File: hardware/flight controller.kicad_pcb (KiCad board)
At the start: 4 copper layers, 50.2 x 98.1 mm, 98 parts, among them J1 Input Power, J10 M8, J11 M9, J12 M10, J13 M11, J14 M12, J15 I2C4, J16 Video In, J17 Video Out, J18 LED Strip, J19 USB_C_Receptacle_USB2.0_16P, J2 M1, J20 UART2, J21 UART7, J22 UART5, J23 UART8, J24 GPIO, J25 SWD, J26 UART3, J27 UART4, J3 M2, J4 M3, J5 M4, J6 M5, J7 M6, J8 Micro_SD_Card, J9 M7, U1 TPS54302, U2 BMP388, U3 QMC5883P, U4 STM32H743VITx, U5 AT7456E, U6 ICM-42688-P, Y1 27MHz, Y2 16MHz, Y3 32.768kHz

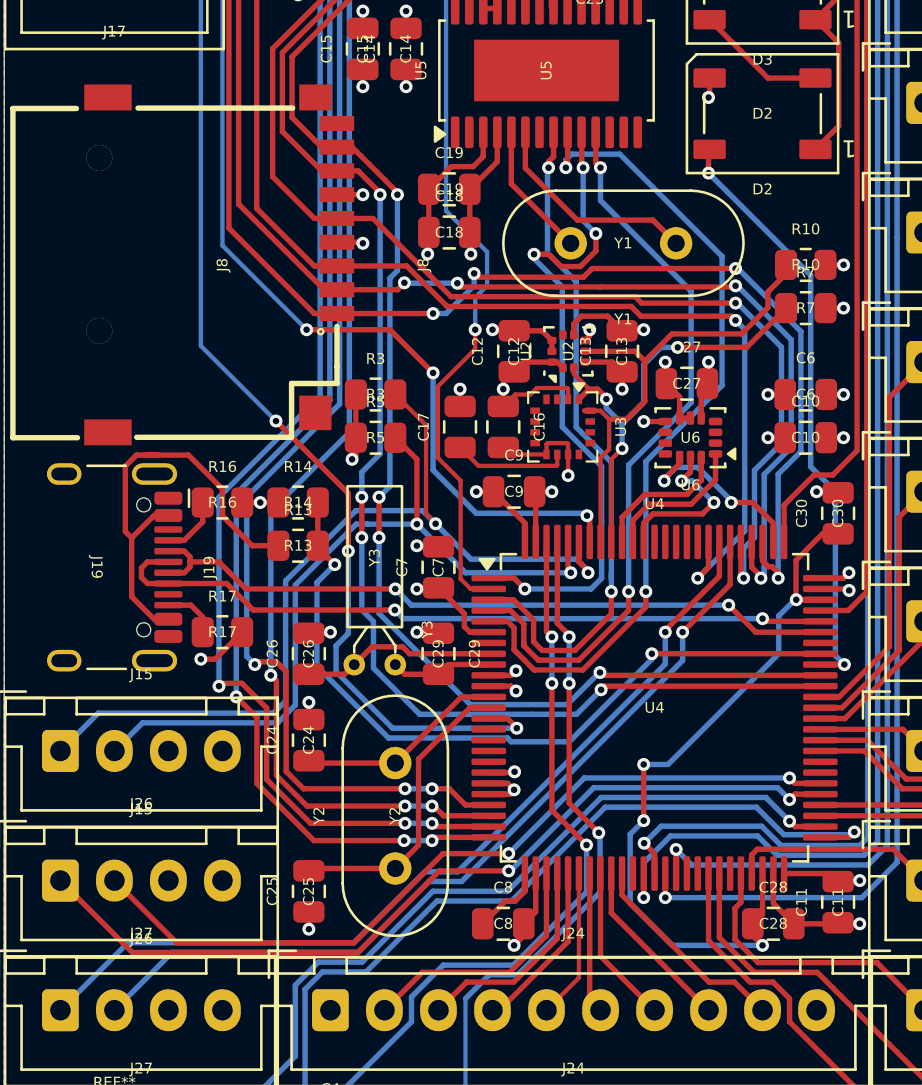
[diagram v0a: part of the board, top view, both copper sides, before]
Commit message: smd crystal
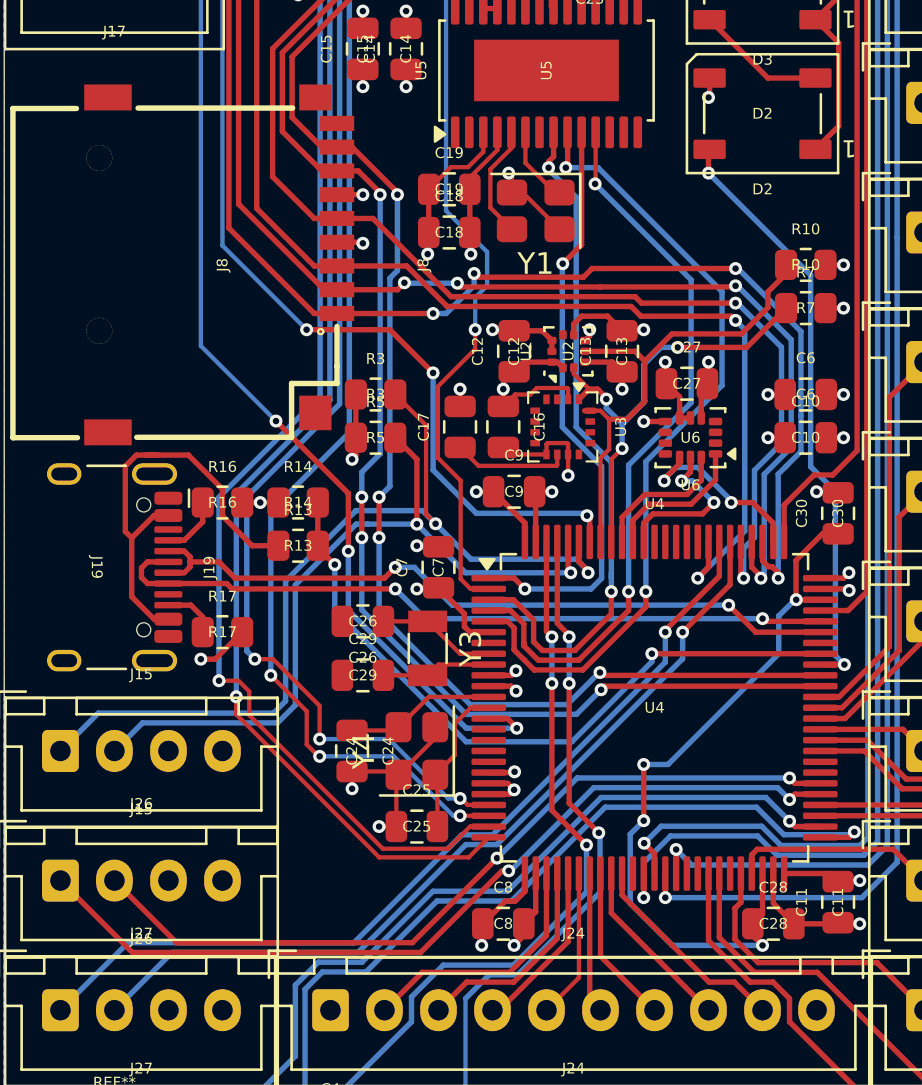
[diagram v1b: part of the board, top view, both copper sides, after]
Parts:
- removed Y2: 16MHz, Crystal:Crystal_HC49-U_Vertical
- added Y4: 16MHz, Crystal:Crystal_SMD_3225-4Pin_3.2x2.5mm, F.Cu at (141.0, 126.5)
- C24, C25: value 33pF -> 12pF
- C26, C29: value 15pF -> 18pF
- Y1: value 27MHz -> Crystal_GND24; footprint Crystal:Crystal_HC49-U_Vertical -> Crystal:Crystal_SMD_3225-4Pin_3.2x2.5mm
- Y3: footprint Crystal:Crystal_DS26_D2.0mm_L6.0mm_Horizontal -> Crystal:Crystal_SMD_3215-2Pin_3.2x1.5mm
- moved Y1 6.67 mm to (146.5, 101.5)
- moved C25 5.83 mm to (141.0, 130.0), turned to 0 degrees
- moved C29 3.64 mm to (138.5, 123.0), turned to 0 degrees
- moved C26 2.92 mm to (138.5, 120.5), turned to 180 degrees
- moved C24 2.06 mm to (138.0, 126.5), turned to -90 degrees
- moved Y3 1.68 mm to (141.5, 121.8), turned to -90 degrees
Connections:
- Y1 pad 2: Net-(U5-CLKIN) -> GND
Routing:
- net GND: track 71.3 -> 81.8 mm
- net /OSC_OUT: track 13.8 -> 7.06 mm
- net Net-(U5-XFB): track 10.1 -> 3.56 mm
- net /OSI_SCK: track 31.1 -> 27.4 mm, vias 4 -> 2
- net /OSC_32_IN: track 8.98 -> 5.50 mm
- net /OSC_IN: track 9.64 -> 6.97 mm
- net /VBUS_SENSE: track 34.8 -> 32.2 mm
- net /NRST: track 77.0 -> 74.6 mm
- net /UART2_CTS: track 91.6 -> 89.6 mm
- net /OSI_MOSI: track 39.0 -> 37.3 mm
- net /UART2_RTS: track 92.7 -> 91.0 mm
- net /SD_D0: track 61.5 -> 60.2 mm
- net Net-(U5-CLKIN): track 6.27 -> 5.31 mm
- net /UART2_TX: track 89.7 -> 89.0 mm, vias 3 -> 1
- net /UART2_RX: track 91.0 -> 90.3 mm, vias 3 -> 1

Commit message: smol
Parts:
- removed C12, C19, C21, C23: 100nF, Capacitor_SMD:C_0805_2012Metric
- removed C18: 1uF, Capacitor_SMD:C_0805_2012Metric
- removed C20: 470uF, Capacitor_THT:CP_Radial_D8.0mm_P3.50mm
- removed C22: 1000uF, Capacitor_THT:CP_Radial_D8.0mm_P3.50mm
- removed R15, R18: 75, Resistor_SMD:R_0805_2012Metric
- removed the REF** at (167.0, 78.5)
- removed the REF** at (167.0, 145.5)
- removed the REF** at (127.0, 145.5)
- removed the REF** at (127.0, 78.5)
- removed U5: AT7456E, Package_SO:TSSOP-28-1EP_4.4x9.7mm_P0.65mm_EP2.85x6.7mm
- removed Y1: Crystal_GND24, Crystal:Crystal_SMD_3225-4Pin_3.2x2.5mm
- added C31: 22uF, Capacitor_SMD:C_1206_3216Metric, B.Cu at (157.5, 60.0)
- added C32: 22uF, Capacitor_SMD:C_1206_3216Metric, B.Cu at (155.0, 60.0)
- added C33: 100nF, Capacitor_SMD:C_0603_1608Metric, B.Cu at (152.0, 63.0)
- added C34: 100nF, Capacitor_SMD:C_0603_1608Metric, B.Cu at (157.0, 69.0)
- added C35: 1uF, Capacitor_SMD:C_0603_1608Metric, B.Cu at (157.0, 70.5)
- added R22: 1K, Resistor_SMD:R_0603_1608Metric, B.Cu at (148.5, 66.0)
- added R23: 75, Resistor_SMD:R_0603_1608Metric, B.Cu at (152.0, 61.5)
- added R24: 75, Resistor_SMD:R_0603_1608Metric, B.Cu at (149.0, 63.0)
- added REF**: MountingHole_2.7mm_M2.5, MountingHole:MountingHole_2.7mm_M2.5, F.Cu at (142.5, 128.0)
- added U7: AT7456ELAH_C42388749, lcsc:LGA-16_L6.8-W4.0-P0.65-TL-2EP, B.Cu at (153.0, 66.1)
- added Y2: Crystal_GND24, Crystal:Crystal_SMD_3225-4Pin_3.2x2.5mm, B.Cu at (153.0, 70.0)
- C1, C13, C14, C15, C16, C27, C3, C6, C7, C8, C9: footprint Capacitor_SMD:C_0805_2012Metric -> Capacitor_SMD:C_0603_1608Metric
- C10, C11, C24, C25, C26, C28, C29, C30: footprint Capacitor_SMD:C_0805_2012Metric -> Capacitor_SMD:C_0603_1608Metric; moved to B.Cu
- D1: value 1N4001 -> SS54; footprint Diode_THT:D_DO-41_SOD81_P7.62mm_Horizontal -> Diode_SMD:D_SMA
- R1, R10, R11, R12, R13, R14, R16, R17, R20, R21, R3, R4, R5, R6, R7, R9: footprint Resistor_SMD:R_0805_2012Metric -> Resistor_SMD:R_0603_1608Metric; moved to B.Cu
- R19, R2, R8: footprint Resistor_SMD:R_0805_2012Metric -> Resistor_SMD:R_0603_1608Metric
- U4, Y3, Y4: moved to B.Cu
- moved C2 87.8 mm to (157.5, 71.5), turned to 180 degrees
- moved U1 84.4 mm to (157.5, 74.5), turned to 180 degrees
- moved C1 82.8 mm to (157.5, 77.0), turned to 180 degrees
- moved L1 78.4 mm to (151.0, 73.0), turned to 180 degrees
- moved C3 77.5 mm to (153.0, 77.5), turned to 0 degrees
- moved J22 75.5 mm to (167.5, 89.5)
- moved D5 75.4 mm to (85.9, 104.1), turned to 0 degrees
- moved J23 75.0 mm to (167.5, 96.0)
- moved R2 75.0 mm to (153.0, 80.5), turned to 0 degrees
- moved R8 73.0 mm to (153.0, 79.0), turned to 180 degrees
- moved D4 72.2 mm to (85.9, 97.5), turned to 0 degrees
- moved D3 71.1 mm to (85.9, 90.9), turned to 0 degrees
- moved J26 69.8 mm to (167.5, 77.5)
- moved J27 69.8 mm to (167.5, 83.5)
- moved C5 69.5 mm to (149.0, 78.0), turned to 0 degrees
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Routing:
- net +3.3V: track 91.6 -> 0.00 mm, vias 28 -> 0
- net /UART2_RTS: track 91.0 -> 0.00 mm, vias 3 -> 0
- net /UART2_RX: track 90.3 -> 0.00 mm, vias 1 -> 0
- net /UART2_CTS: track 89.6 -> 0.00 mm, vias 3 -> 0
- net /UART2_TX: track 89.0 -> 0.00 mm, vias 1 -> 0
- net /SWDIO: track 86.8 -> 0.00 mm
- net /SWCLK: track 82.8 -> 0.00 mm, vias 1 -> 0
- net GND: track 81.8 -> 0.00 mm, vias 37 -> 0
- net /UART7_RX: track 75.1 -> 0.00 mm, vias 1 -> 0
- net /NRST: track 74.6 -> 0.00 mm, vias 4 -> 0
- net /UART7_TX: track 73.8 -> 0.00 mm, vias 1 -> 0
- net /UART7_RTS: track 73.4 -> 0.00 mm, vias 1 -> 0
- net /UART7_CTS: track 71.8 -> 0.00 mm, vias 1 -> 0
- net /BOOT0: track 67.7 -> 0.00 mm, vias 4 -> 0
- net /SD_D2: track 60.9 -> 0.00 mm, vias 4 -> 0
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- removed copper zone on In2.Cu, net +3.3V
- removed copper zone on In2.Cu, net +5V
- removed copper zone on B.Cu, net GND
- removed copper zone on F.Cu, net GND
- removed copper zone on In1.Cu, net GND
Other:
- board size 50.2 x 98.1 mm -> 40 x 86.5 mm
- board text removed: "flight controller"

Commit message: idk
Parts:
- C6: moved to B.Cu
- moved R9 8.49 mm to (133.5, 89.5)
- moved R11 7.65 mm to (132.0, 91.0)
- moved R1 5.83 mm to (134.5, 87.5)
- moved C28 1.00 mm to (140.5, 87.5)
- moved C6 0.50 mm to (158.0, 81.0)
- moved C9 0.25 mm to (158.0, 97.8)
- moved U4 0.18 mm to (151.5, 90.5)
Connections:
- U4 pad 28: /A1 -> /A8
- U4 pad 29: /A2 -> /A7
- U4 pad 30: /A3 -> /A6
- U4 pad 31: /A4 -> /A1
- U4 pad 33: /A6 -> /A2
- U4 pad 34: /A7 -> /A4
- U4 pad 35: /A8 -> /A3
- U4 pad 43: /M1 -> /M4
- U4 pad 44: /M2 -> /M8
- U4 pad 46: /M3 -> /M10
- U4 pad 47: /M4 -> /M12
- U4 pad 61: /M5 -> /M1
- U4 pad 62: /M6 -> /M5
- U4 pad 63: /M7 -> /M9
- U4 pad 64: /M8 -> /M11

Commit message: some routing
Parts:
- J21: value UART7 -> UART3
- J26: value UART3 -> UART6
- moved C16 8.50 mm to (156.0, 86.5)
- moved C17 8.50 mm to (159.0, 84.0)
- moved U3 8.50 mm to (156.0, 84.0)
- moved C27 5.22 mm to (160.0, 80.0)
- moved U6 5.22 mm to (157.5, 80.0)
- moved U2 4.26 mm to (155.5, 93.0), turned to 180 degrees
- moved C13 3.54 mm to (155.5, 95.0), turned to 0 degrees
- moved J19 0.62 mm to (141.0, 76.0)
- moved J8 0.53 mm to (146.9, 90.5)
- moved C11 0.50 mm to (142.0, 83.5)
- moved R10 0.50 mm to (155.5, 79.5)
- moved R13 0.50 mm to (140.0, 79.0)
- moved R14 0.50 mm to (138.5, 79.0)
- moved R17 0.50 mm to (142.5, 78.5)
- moved R7 0.50 mm to (154.0, 79.5)
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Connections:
- J21 pad 1: /UART7_TX -> /UART3_TX
- J21 pad 2: /UART7_RX -> /UART3_RX
- J21 pad 3: /UART7_CTS -> /UART3_CTS
- J21 pad 4: /UART7_RTS -> /UART3_RTS
- J26 pad 1: /UART3_TX -> /UART6_TX
- J26 pad 2: /UART3_RX -> /UART6_RX
- U4 pad 22: /UART2_CTS -> /M4
- U4 pad 23: /UART2_RTS -> /M8
- U4 pad 24: /UART2_TX -> /M10
- U4 pad 25: /UART2_RX -> /M12
- U4 pad 37: /UART7_RX -> unconnected-(U4-PE7-Pad37)
- U4 pad 38: /UART7_TX -> unconnected-(U4-PE8-Pad38)
- U4 pad 39: /UART7_RTS -> /M3
- U4 pad 40: /UART7_CTS -> unconnected-(U4-PE10-Pad40)
- U4 pad 41: unconnected-(U4-PE11-Pad41) -> /M7
- U4 pad 43: /M4 -> /M2
- U4 pad 44: /M8 -> /M6
- U4 pad 46: /M10 -> /M11
- U4 pad 47: /M12 -> /M9
- U4 pad 53: /M12 -> /M1
- U4 pad 54: /M11 -> /M5
- U4 pad 58: unconnected-(U4-PD11-Pad58) -> /UART3_CTS
- U4 pad 59: /M10 -> /UART3_RTS
- U4 pad 60: /M9 -> unconnected-(U4-PD13-Pad60)
- U4 pad 61: /M1 -> unconnected-(U4-PD14-Pad61)
- U4 pad 62: /M5 -> unconnected-(U4-PD15-Pad62)
- U4 pad 63: /M9 -> /UART6_TX
- U4 pad 64: /M11 -> /UART6_RX
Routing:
- net /M12: track 0.00 -> 44.8 mm
- net /M11: track 0.00 -> 42.4 mm, vias 0 -> 1
- net /M10: track 0.00 -> 31.9 mm
- net /M9: track 0.00 -> 28.9 mm, vias 0 -> 1
- net /M8: track 0.00 -> 26.5 mm
- net /M7: track 0.00 -> 24.0 mm, vias 0 -> 1
- net /M5: track 0.00 -> 23.0 mm
- net /M6: track 0.00 -> 22.1 mm, vias 0 -> 1
- net GND: track 0.00 -> 21.0 mm, vias 0 -> 7
- net /M4: track 0.00 -> 20.6 mm
- net +3.3V: track 0.00 -> 20.3 mm, vias 0 -> 6
- net /M3: track 0.00 -> 17.9 mm, vias 0 -> 1
- net /IMU_CS: track 0.00 -> 17.8 mm, vias 0 -> 1
- net /I2C_SCL: track 0.00 -> 17.4 mm, vias 0 -> 2
- net /A1: track 0.00 -> 17.4 mm
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
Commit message: more routing
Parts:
- moved R2 1.50 mm to (153.0, 79.0)
- moved R8 1.50 mm to (153.0, 80.5)
- moved R16 1.27 mm to (142.2, 74.8)
- moved R17 0.79 mm to (142.2, 77.8)
- moved L1 0.50 mm to (150.5, 73.0)
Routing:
- net +3.3V: track 20.3 -> 30.2 mm, vias 6 -> 8
- net Net-(U1-SW): track 0.00 -> 9.29 mm
- net Net-(U1-FB): track 0.00 -> 8.27 mm
- net GND: track 21.0 -> 27.4 mm, vias 7 -> 10
- net +5V: track 0.00 -> 3.18 mm, vias 0 -> 1
- net Net-(U1-BOOT): track 0.00 -> 1.70 mm
- net Net-(J19-CC1): track 0.00 -> 1.68 mm, vias 0 -> 1
- net Net-(J19-CC2): track 0.00 -> 1.67 mm, vias 0 -> 1
- net /M3: track 17.9 -> 19.0 mm
- net /USB_DP: track 13.0 -> 13.9 mm
- net /USB_DN: track 16.5 -> 17.2 mm

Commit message: finish v2
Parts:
- removed the D3 at (85.9, 90.9)
- removed D4, D5: WS2812B, LED_SMD:LED_WS2812B_PLCC4_5.0x5.0mm_P3.2mm
- added REF**: MountingHole_2.7mm_M2.5, MountingHole:MountingHole_2.7mm_M2.5, F.Cu at (142.5, 60.0)
- added REF**: MountingHole_2.7mm_M2.5, MountingHole:MountingHole_2.7mm_M2.5, F.Cu at (172.5, 127.5)
- added REF**: MountingHole_2.7mm_M2.5, MountingHole:MountingHole_2.7mm_M2.5, F.Cu at (172.5, 60.0)
- R10, R7: moved to F.Cu
- Y1: renamed from Y2; value Crystal_GND24 -> 27MHz
- moved J23 18.0 mm to (167.5, 78.0)
- moved R7 15.1 mm to (162.5, 92.0), turned to 0 degrees
- moved R10 13.0 mm to (162.5, 90.5), turned to 0 degrees
- moved J26 12.5 mm to (167.5, 90.0)
- moved R1 9.86 mm to (139.5, 96.0)
- moved R19 8.34 mm to (141.0, 69.5), turned to 90 degrees
- moved R11 7.57 mm to (139.5, 90.0)
- moved J20 6.50 mm to (162.5, 72.0)
- moved J22 6.50 mm to (167.5, 96.0)
- moved R9 6.08 mm to (139.5, 88.5)
- moved J21 5.53 mm to (162.5, 66.0)
- moved R18 5.30 mm to (143.0, 69.5), turned to 90 degrees
- moved C26 5.10 mm to (139.5, 82.5)
- moved R15 4.92 mm to (140.5, 74.5), turned to 180 degrees
- moved R16 4.24 mm to (152.0, 60.0)
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- renumbered C13 to C12, C16 to C13, C17 to C16, C35 to C17, C34 to C18, C31 to C19, C32 to C20, C33 to C21, C24 to C22, C25 to C23, C26 to C24, C27 to C25, C28 to C26, C29 to C27, C30 to C28, D6 to D3, R23 to R14, R14 to R15, R24 to R16, R22 to R17, R16 to R18, R17 to R19, R19 to R20, R20 to R21, R21 to R22, U7 to U5, Y4 to Y2
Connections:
- J18 pad 1: Net-(D5-DOUT) -> Net-(D2-DOUT)
- U4 pad 2: /ARM_LED -> unconnected-(U4-PE3-Pad2)
- U4 pad 22: /M4 -> /M12
- U4 pad 23: /M8 -> /M10
- U4 pad 24: /M10 -> /M8
- U4 pad 25: /M12 -> /M4
- U4 pad 7: unconnected-(U4-PC13-Pad7) -> /ARM_LED
- U4 pad 84: unconnected-(U4-PD3-Pad84) -> /UART2_CTS
- U4 pad 85: unconnected-(U4-PD4-Pad85) -> /UART2_RTS
- U4 pad 86: unconnected-(U4-PD5-Pad86) -> /UART2_TX
- U4 pad 87: unconnected-(U4-PD6-Pad87) -> /UART2_RX
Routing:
- net +3.3V: track 30.2 -> 97.3 mm, vias 8 -> 22
- net /UART3_RTS: track 0.00 -> 59.1 mm, vias 0 -> 2
- net /UART3_CTS: track 0.00 -> 58.8 mm, vias 0 -> 2
- net /UART3_RX: track 0.00 -> 58.7 mm, vias 0 -> 2
- net /UART3_TX: track 0.00 -> 57.8 mm, vias 0 -> 2
- net GND: track 27.4 -> 82.2 mm, vias 10 -> 32
- net /SWDIO: track 0.00 -> 54.5 mm, vias 0 -> 3
- net /NRST: track 0.00 -> 52.8 mm, vias 0 -> 2
- net /OSI_MOSI: track 0.00 -> 51.1 mm, vias 0 -> 2
- net /SWCLK: track 0.00 -> 46.5 mm, vias 0 -> 1
- net /BOOT0: track 0.00 -> 44.9 mm
- net /UART4_RX: track 0.00 -> 43.8 mm, vias 0 -> 1
- net /OSI_MISO: track 0.00 -> 43.5 mm, vias 0 -> 2
- net /UART4_TX: track 0.00 -> 41.4 mm, vias 0 -> 1
- net /UART6_RX: track 0.00 -> 37.5 mm, vias 0 -> 1
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- added copper zone on In2.Cu, net +3.3V
- added copper zone on In2.Cu, net +5V
- added copper zone on B.Cu, net GND
- added copper zone on F.Cu, net GND
- added copper zone on In1.Cu, net GND
